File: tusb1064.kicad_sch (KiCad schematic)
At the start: 28 parts, among them U13 TUSB1064RNQT

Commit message: Preliminary Revision of PS176 DP->HDMI Subsystem
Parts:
- removed R53: 100k, Resistor_SMD:R_0402_1005Metric, symbol JLCImport:0402WGF1003TCE
- added DNP1: 100k, Resistor_SMD:R_01005_0402Metric, symbol Device:R
- added R54, R55: 3.3k, Resistor_SMD:R_0402_1005Metric, symbol JLCImport:0402WGF3301TCE
- added R59, R60: 1M, Resistor_SMD:R_0402_1005Metric, symbol JLCImport:0402WGF1004TCE
- renumbered DNP to DNP0
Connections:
- net CTRL_SCL: now also U13.21 (FLIP/SCL), R54.1
- net CTRL_SDA: now also R55.1
- net DP_HPD: now also DNP1.1
- net GND: now also DNP1.2, R59.1
- net at C87.1, U13.27 (AUXn): now also R59.2
- net at C88.1, U13.26 (AUXp): now also R60.2
- new net CTRL_LDO_3V3: R54.2, R55.2
- new net PS_VDD33: R60.1
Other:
- note added: "100k pull down prob not needed bc of internal 500k pull down; EVM labels as DNP"
- note removed: "100k pull down required per DP spec; check this again to make sure"
- moved on the sheet: C67, C68, C69, C70, C71, C72, C73, C74, C75, C76, C77, C78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

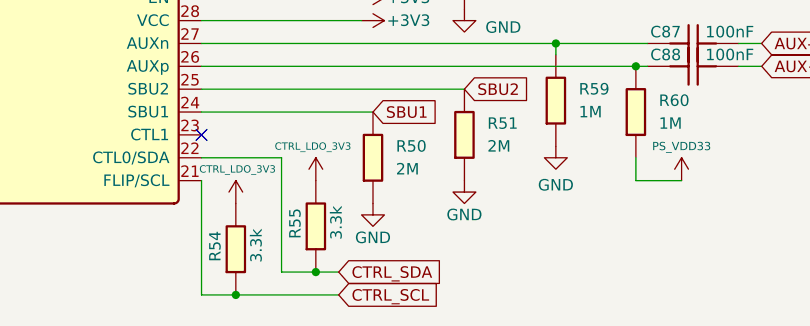
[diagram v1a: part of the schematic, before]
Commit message: Preliminary draft of USB controller and power circuit
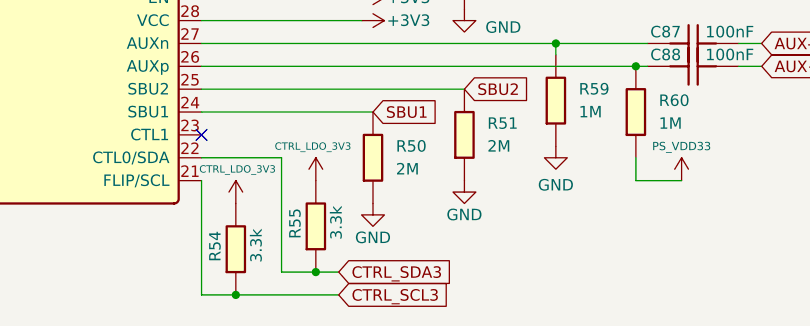
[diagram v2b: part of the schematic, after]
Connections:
- net CTRL_SCL renamed CTRL_SCL3
- net CTRL_SDA renamed CTRL_SDA3
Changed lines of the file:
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@@
 		)
 	)
-	(global_label "CTRL_SDA"
+	(global_label "CTRL_SDA3"
 		(shape input)
 		(at 118.11 95.25 0)
@@
 		)
 		(property "Intersheetrefs" "${INTERSHEET_REFS}"
-			(at 130.1666 95.25 0)
+			(at 131.3761 95.25 0)
 			(hide yes)
 			(show_name no)
@@
 		)
 	)
-	(global_label "CTRL_SCL"
+	(global_label "CTRL_SCL3"
 		(shape input)
 		(at 118.11 97.79 0)
@@
 		)
 		(property "Intersheetrefs" "${INTERSHEET_REFS}"
-			(at 130.1061 97.79 0)
+			(at 131.3156 97.79 0)
 			(hide yes)
 			(show_name no)

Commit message: Preliminary design of USB2244i USB2.0 -> SD converter
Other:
- company: (none) -> Designed by: Matthew Kong
- title: (none) -> TUSB1064 - USB-C DP alt mode 10Gbps switch
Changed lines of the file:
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@@
 	(generator_version "10.0")
 	(paper "A5")
+	(title_block
+		(title "TUSB1064 - USB-C DP alt mode 10Gbps switch")
+		(date "2026-07-09")
+		(rev "1.0")
+		(company "Designed by: Matthew Kong")
+	)
 	(rectangle
 		(start 36.83 43.18)

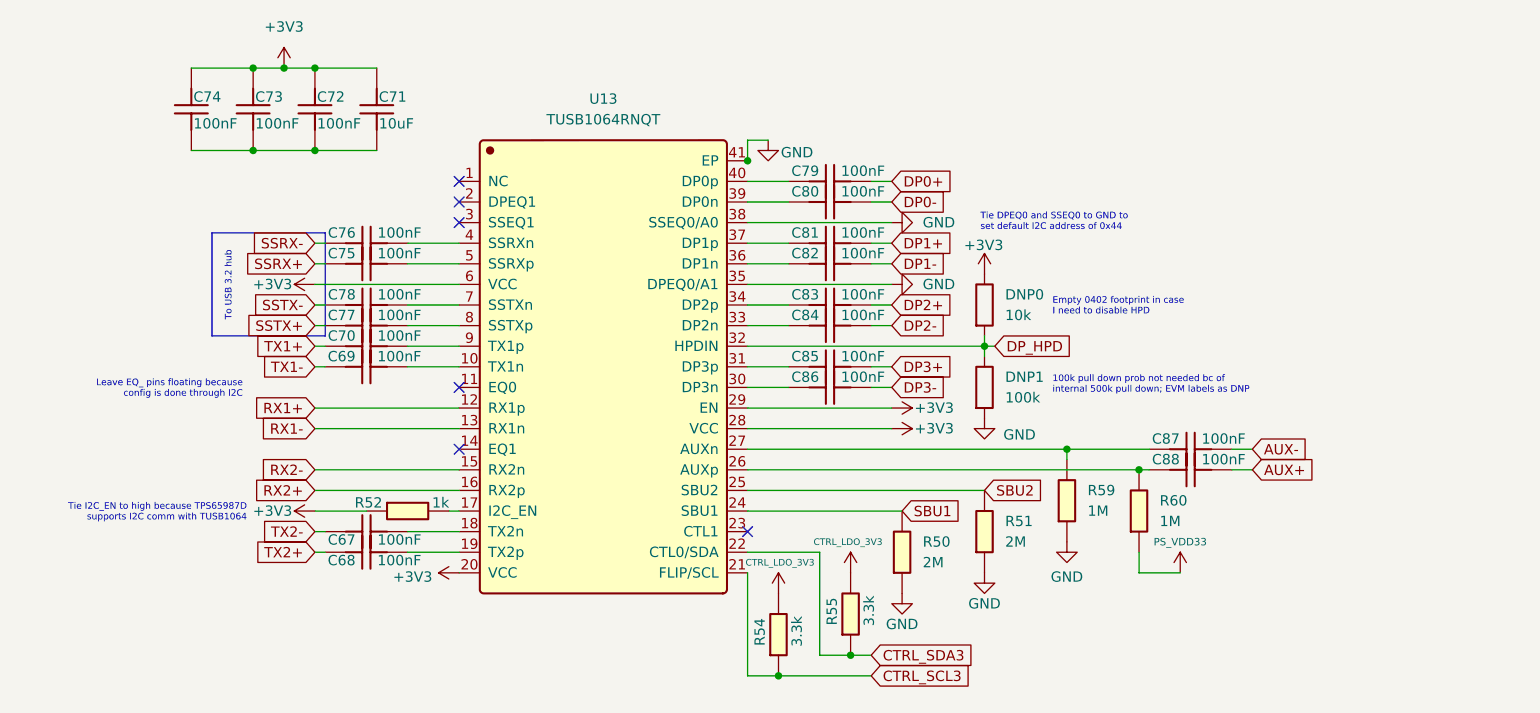
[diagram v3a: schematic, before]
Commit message: Mostly complete initial transfer to hierarchical schematic
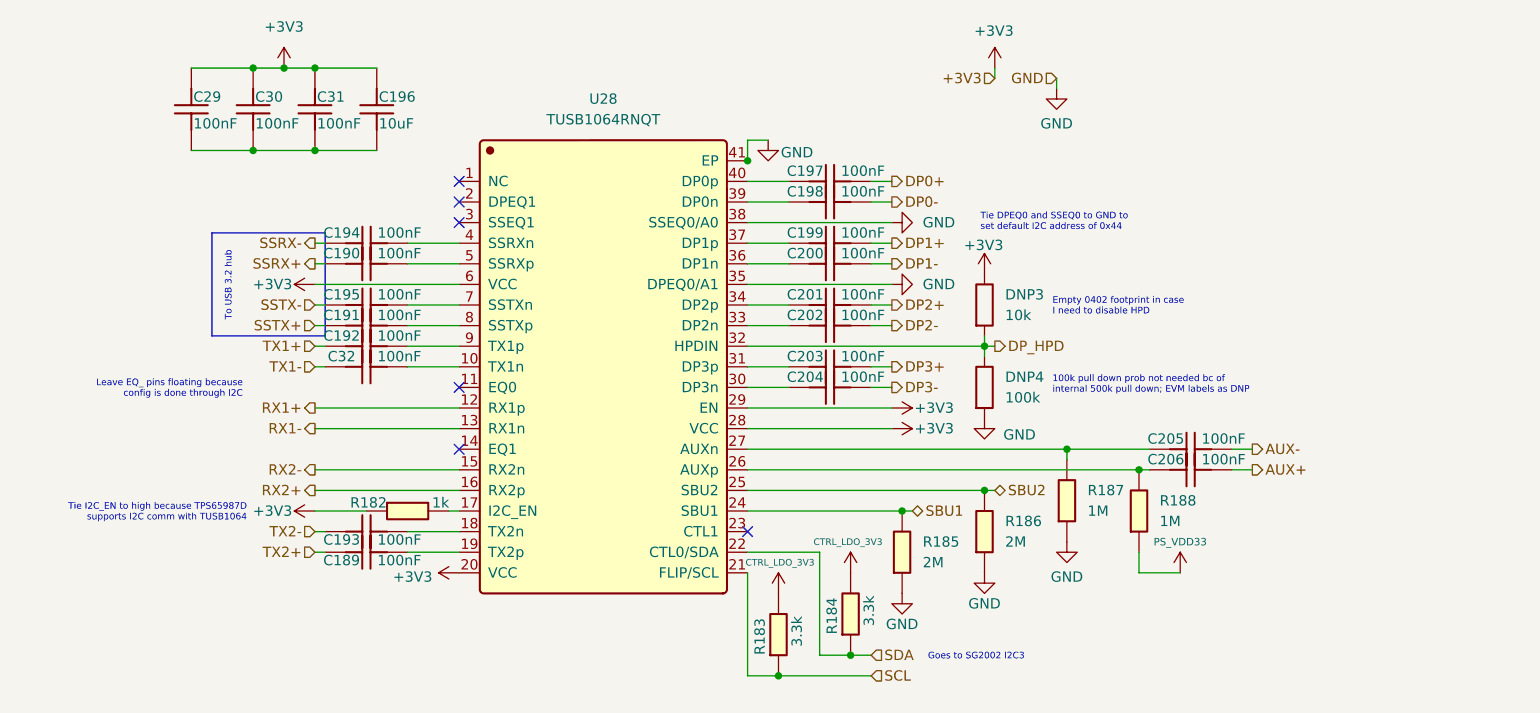
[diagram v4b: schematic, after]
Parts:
- renumbered C68 to C189, C75 to C190, C77 to C191, C70 to C192, C67 to C193, C76 to C194, C78 to C195, C71 to C196, C79 to C197, C80 to C198, C81 to C199, C82 to C200, C83 to C201, C84 to C202, C85 to C203, C86 to C204, C87 to C205, C88 to C206, C74 to C29, C73 to C30, C72 to C31, C69 to C32, DNP0 to DNP3, DNP1 to DNP4, R52 to R182, R54 to R183, R55 to R184, R50 to R185, R51 to R186, R59 to R187, R60 to R188, U13 to U28
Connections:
- net CTRL_SCL3 renamed SCL
- net CTRL_SDA3 renamed SDA
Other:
- note added: "Goes to SG2002 I2C3"

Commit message: Added TVS clamping diodes to upstream USB-C port and fixed RX/TX orientation routing for entire system
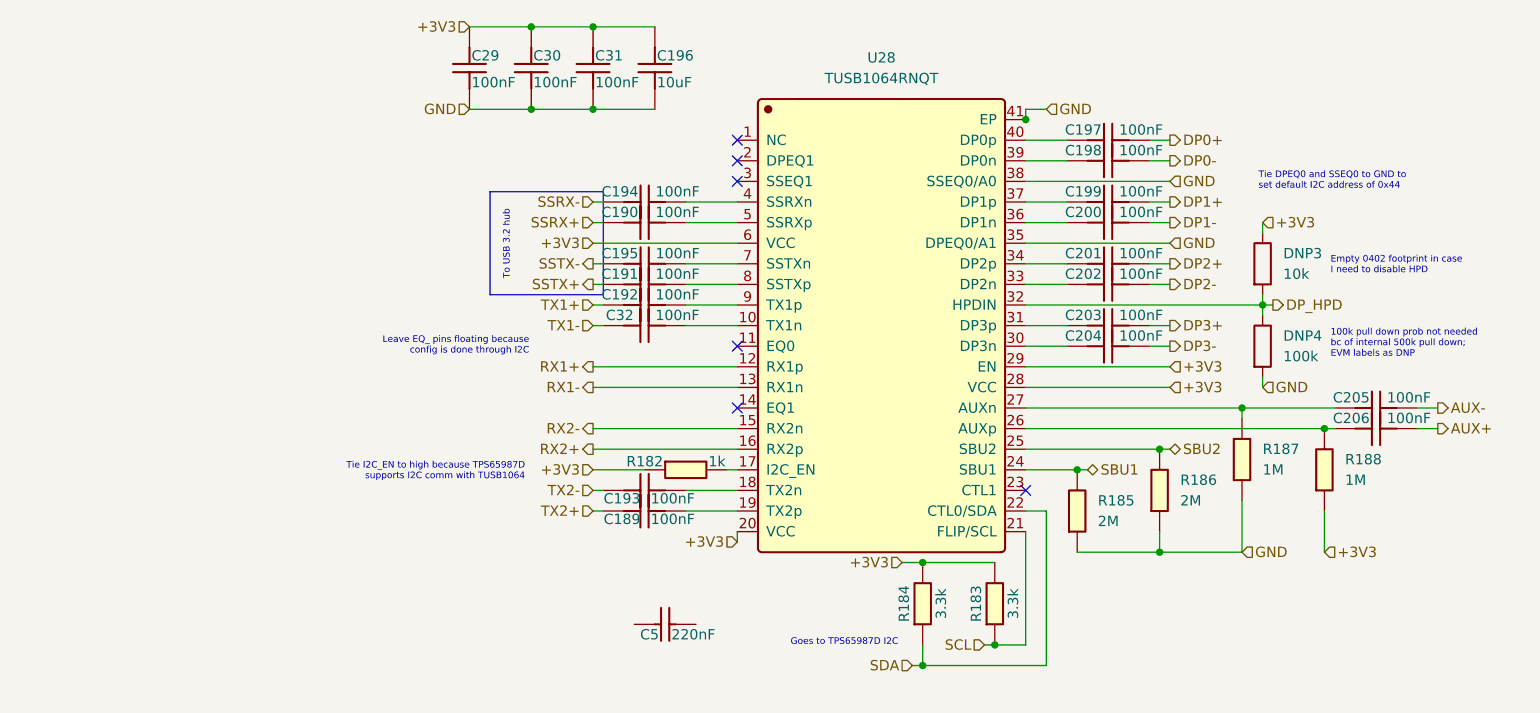
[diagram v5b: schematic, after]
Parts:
- added C5: 220nF, Capacitor_SMD:C_0402_1005Metric, symbol JLCImport:CL05B224KO5NNNC
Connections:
- net CTRL_LDO_3V3 is gone; now on net +3V3: R183.2, R184.2
- net PS_VDD33 is gone; now on net +3V3: R188.1
- net GND: now also C196.1, C29.1, C30.1, C31.1
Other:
- note added: "Goes to TPS65987D I2C"
- note removed: "Goes to SG2002 I2C3"
- moved on the sheet: C189, C190, C191, C192, C193, C194, C195, C196, C197, C198, C199, C200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

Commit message: Basic Function Review and Documentation for TUSB1064 subsystem
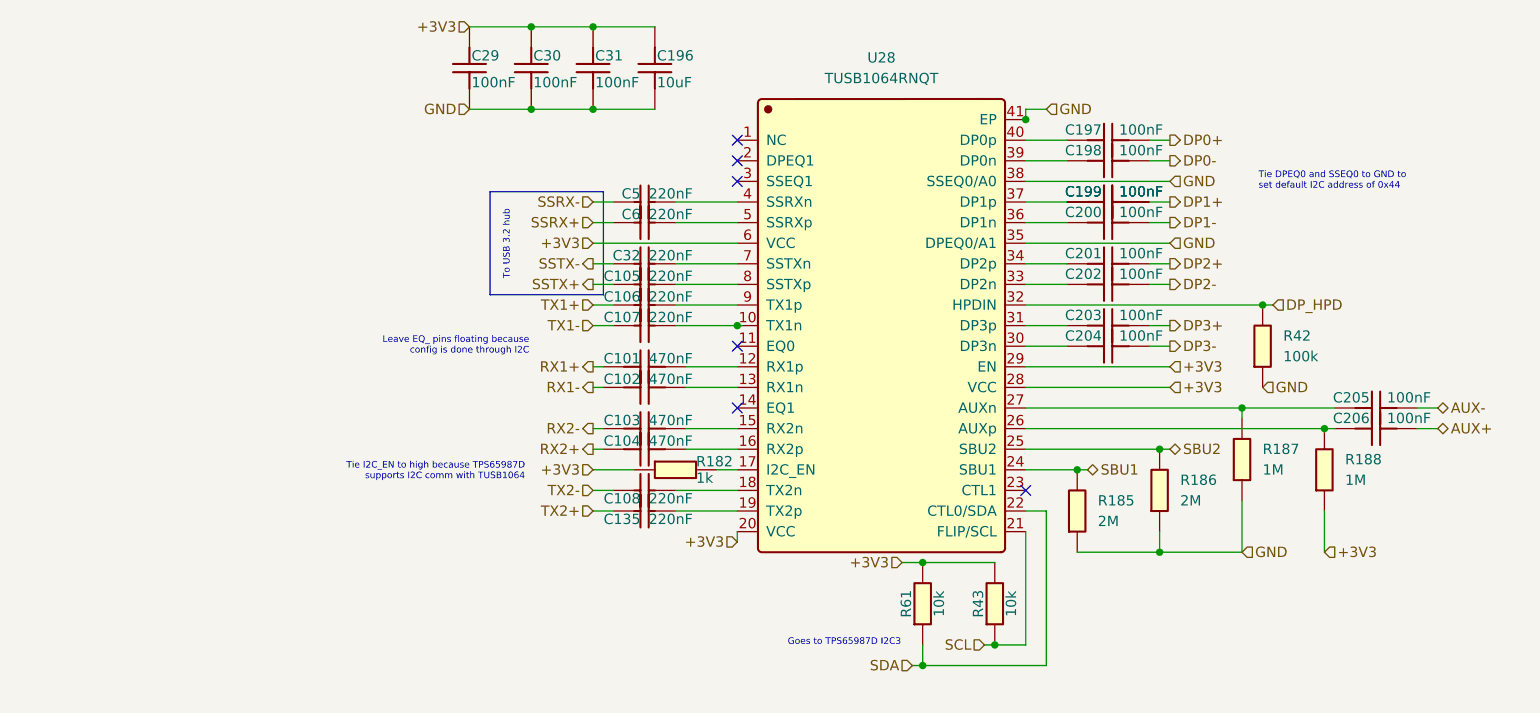
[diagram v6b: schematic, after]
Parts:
- removed C189, C190, C191, C192, C193, C194, C195, C32: 100nF, Capacitor_SMD:C_0402_1005Metric, symbol JLCImport:CL05B104KB54PNC
- removed DNP3: 10k, Resistor_SMD:R_01005_0402Metric, symbol Device:R
- removed DNP4: 100k, Resistor_SMD:R_01005_0402Metric, symbol Device:R
- removed R183, R184: 3.3k, Resistor_SMD:R_0402_1005Metric, symbol JLCImport:0402WGF3301TCE
- added C101, C102, C103, C104: 470nF, Capacitor_SMD:C_0402_1005Metric, symbol JLCImport:TCC0402X5R474M160AT
- added C105, C106, C107, C108, C135, C32, C6: 220nF, Capacitor_SMD:C_0402_1005Metric, symbol JLCImport:CL05B224KO5NNNC
- added R42: 100k, Resistor_SMD:R_0402_1005Metric, symbol JLCImport:0402WGF1003TCE
- added R43, R61: 10k, Resistor_SMD:R_0402_1005Metric, symbol JLCImport:0402WGF1002TCE
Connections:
- net +3V3: now also R43.2, R61.2
- net DP_HPD: now also R42.2
- net GND: now also R42.1
- net RX1+: now also C101.1; no longer U28.12 (RX1p)
- net RX1-: now also C102.1; no longer U28.13 (RX1n)
- net RX2+: now also C104.1; no longer U28.16 (RX2p)
- net RX2-: now also C103.1; no longer U28.15 (RX2n)
- net SCL: now also R43.1
- net SDA: now also R61.1
- net SSRX+: now also C6.1
- net SSRX-: now also C5.1
- net SSTX+: now also C105.1
- net SSTX-: now also C32.1
- net TX1+: now also C106.1
- net TX1-: now also C107.1
- net TX2+: now also C135.1
- net TX2-: now also C108.1
- net at U28.9 (TX1p): now also C106.2
- net at U28.10 (TX1n): now also C107.2
- net at U28.18 (TX2n): now also C108.2
- net at U28.7 (SSTXn): now also C32.2
- net at U28.19 (TX2p): now also C135.2
- net at U28.4 (SSRXn): now also C5.2
- net at U28.5 (SSRXp): now also C6.2
- net at U28.8 (SSTXp): now also C105.2
- new net: C104.2, U28.16 (RX2p)
- new net: C102.2, U28.13 (RX1n)
- new net: C101.2, U28.12 (RX1p)
- new net: C103.2, U28.15 (RX2n)
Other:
- note added: "Goes to TPS65987D I2C3"
- note removed: "100k pull down prob not needed bc of internal 500k pull down; EVM labels as DNP"
- note removed: "Empty 0402 footprint in case I need to disable HPD"
- note removed: "Goes to TPS65987D I2C"
- moved on the sheet: R182

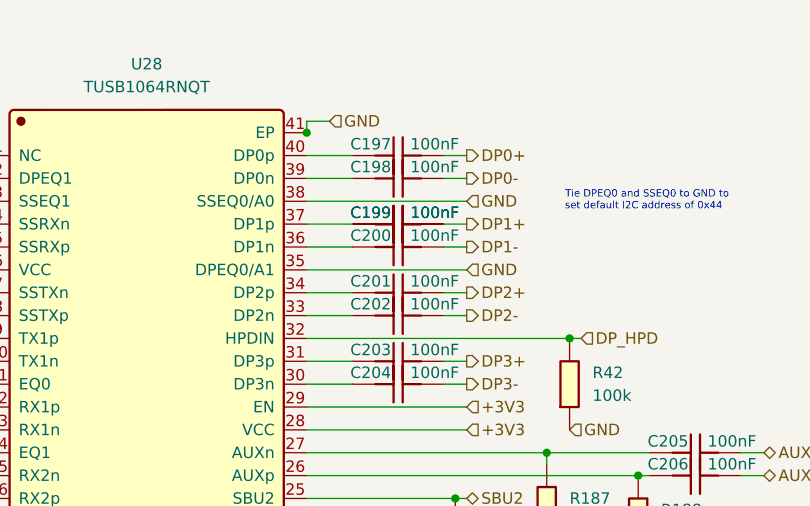
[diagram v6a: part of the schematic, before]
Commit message: Small bug fixes to LT6911C subsystem to match official adapter model
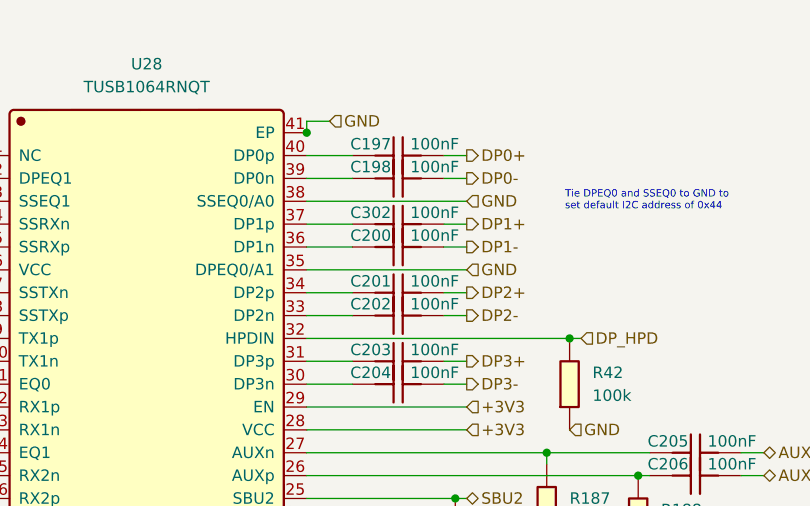
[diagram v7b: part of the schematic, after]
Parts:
- removed C199: 100nF, Capacitor_SMD:C_0402_1005Metric, symbol JLCImport:CL05B104KB54PNC
- added C302: 100nF, Capacitor_SMD:C_0402_1005Metric, symbol JLCImport:CL05B104KB54PNC
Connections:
- net DP1+: now also C302.2
- net at U28.37 (DP1p): now also C302.1
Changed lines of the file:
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@@
 	(title_block
 		(title "TUSB1064 - USB-C DP alt mode 10Gbps switch")
-		(date "2026-07-09")
-		(rev "1.0")
+		(date "2026-07-22")
+		(rev "1.1")
 		(company "Designed by: Matthew Kong")
 	)
@@
 		(in_pos_files yes)
 		(dnp no)
-		(property "Reference" "C199"
+		(property "Reference" "C302"
 			(at 144.272 38.1 0)
 			(show_name no)
@@
 			(project "serverv2_backplane"
 				(path "/d38d6818-cf53-410d-afa3-a75a85b7c05a/348ac17a-b6bd-48ae-9df8-a4f850725408"
-					(reference "C199")
-					(unit 1)
-				)
-			)
-		)
-	)
-	(symbol
-		(lib_id "JLCImport:CL05B104KB54PNC")
-		(at 147.32 39.37 0)
-		(unit 1)
-		(body_style 1)
-		(exclude_from_sim no)
-		(in_bom yes)
-		(on_board yes)
-		(in_pos_files yes)
-		(dnp no)
-		(property "Reference" "C199"
-			(at 144.272 38.1 0)
-			(show_name no)
-			(do_not_autoplace no)
-			(effects
-				(font
-					(size 1.27 1.27)
-				)
-			)
-		)
-		(property "Value" "100nF"
-			(at 151.384 38.1 0)
-			(show_name no)
-			(do_not_autoplace no)
-			(effects
-				(font
-					(size 1.27 1.27)
-				)
-			)
-		)
-		(property "Footprint" "Capacitor_SMD:C_0402_1005Metric"
-			(at 147.32 39.37 0)
-			(hide yes)
-			(show_name no)
-			(do_not_autoplace no)
-			(effects
-				(font
-					(size 1.27 1.27)
-				)
-			)
-		)
-		(property "Datasheet" "https://www.lcsc.com/datasheet/lcsc_datasheet_2304140030_Samsung-Electro-Mechanics-CL05B104KB54PNC_C307331.pdf"
-			(at 147.32 39.37 0)
-			(hide yes)
-			(show_name no)
-			(do_not_autoplace no)
-			(effects
-				(font
-					(size 1.27 1.27)
-				)
-			)
-		)
-		(property "Description" "100nF 50V X7R ±10% 0402 Multilayer Ceramic Capacitors MLCC - SMD/SMT ROHS"
-			(at 147.32 39.37 0)
-			(hide yes)
-			(show_name no)
-			(do_not_autoplace no)
-			(effects
-				(font
-					(size 1.27 1.27)
-				)
-			)
-		)
-		(property "LCSC" "C307331"
-			(at 147.32 39.37 0)
-			(hide yes)
-			(show_name no)
-			(do_not_autoplace no)
-			(effects
-				(font
-					(size 1.27 1.27)
-				)
-			)
-		)
-		(property "Manufacturer" "Samsung Electro-Mechanics"
-			(at 147.32 39.37 0)
-			(hide yes)
-			(show_name no)
-			(do_not_autoplace no)
-			(effects
-				(font
-					(size 1.27 1.27)
-				)
-			)
-		)
-		(property "Manufacturer Part" "CL05B104KB54PNC"
-			(at 147.32 39.37 0)
-			(hide yes)
-			(show_name no)
-			(do_not_autoplace no)
-			(effects
-				(font
-					(size 1.27 1.27)
-				)
-			)
-		)
-		(pin "1"
-		)
-		(pin "2"
-		)
-		(instances
-			(project "serverv2_backplane"
-				(path "/d38d6818-cf53-410d-afa3-a75a85b7c05a/348ac17a-b6bd-48ae-9df8-a4f850725408"
-					(reference "C199")
+					(reference "C302")
 					(unit 1)
 				)
